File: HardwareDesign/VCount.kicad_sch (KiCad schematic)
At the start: 10 parts, among them SW201 SW_DIP_x10, U202 GAL22V10, U203 74ACT163, U204 74ACT163, U205 74ACT163

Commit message: don't incr upper VCOUNT counters unless HCEND is asserted
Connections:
- net HCOUNT_END: now also U204.10 (CET), U205.10 (CET)
- net at U204.15 (TC), U205.7 (CEP): no longer U205.10 (CET)
- net at U203.15 (TC), U204.7 (CEP): no longer U204.10 (CET)
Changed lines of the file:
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@@
-	)
-	(junction
-		(at 124.46 86.36)
-		(diameter 0)
-		(color 0 0 0 0)
 	)
 	(junction
@@
 	)
 	(junction
-		(at 72.39 86.36)
-		(diameter 0)
-		(color 0 0 0 0)
-	)
-	(junction
 		(at 143.51 76.2)
 		(diameter 0)
@@
 	)
 	(junction
+		(at 140.97 134.62)
+		(diameter 0)
+		(color 0 0 0 0)
+	)
+	(junction
 		(at 38.1 118.11)
 		(diameter 0)
@@
 	(junction
 		(at 143.51 132.08)
+		(diameter 0)
+		(color 0 0 0 0)
+	)
+	(junction
+		(at 88.9 134.62)
 		(diameter 0)
 		(color 0 0 0 0)
@@
 	(wire
 		(pts
-			(xy 93.98 88.9) (xy 72.39 88.9)
-		)
-		(stroke
-			(width 0)
-			(type default)
-		)
-	)
-	(wire
-		(pts
 			(xy 200.66 86.36) (xy 205.74 86.36)
 		)
@@
 	(wire
 		(pts
+			(xy 93.98 88.9) (xy 88.9 88.9)
+		)
+		(stroke
+			(width 0)
+			(type default)
+		)
+	)
+	(wire
+		(pts
 			(xy 66.04 91.44) (xy 66.04 118.11)
 		)
@@
 	(wire
 		(pts
-			(xy 124.46 86.36) (xy 124.46 88.9)
-		)
-		(stroke
-			(width 0)
-			(type default)
-		)
-	)
-	(wire
-		(pts
 			(xy 54.61 24.13) (xy 54.61 27.94)
 		)
@@
 	(wire
 		(pts
-			(xy 124.46 88.9) (xy 146.05 88.9)
-		)
-		(stroke
-			(width 0)
-			(type default)
-		)
-	)
-	(wire
-		(pts
 			(xy 91.44 132.08) (xy 143.51 132.08)
 		)
@@
 	(wire
 		(pts
+			(xy 140.97 88.9) (xy 140.97 134.62)
+		)
+		(stroke
+			(width 0)
+			(type default)
+		)
+	)
+	(wire
+		(pts
 			(xy 24.765 24.13) (xy 40.005 24.13)
 		)
@@
 		)
 	)
-	(wire
-		(pts
-			(xy 72.39 88.9) (xy 72.39 86.36)
-		)
-		(stroke
-			(width 0)
-			(type default)
-		)
-	)
 	(bus
 		(pts
@@
 		)
 	)
+	(wire
+		(pts
+			(xy 146.05 88.9) (xy 140.97 88.9)
+		)
+		(stroke
+			(width 0)
+			(type default)
+		)
+	)
 	(bus
 		(pts
@@
 	(wire
 		(pts
-			(xy 33.02 134.62) (xy 184.15 134.62)
+			(xy 33.02 134.62) (xy 88.9 134.62)
 		)
 		(stroke
@@
 	(wire
 		(pts
+			(xy 88.9 88.9) (xy 88.9 134.62)
+		)
+		(stroke
+			(width 0)
+			(type default)
+		)
+	)
+	(wire
+		(pts
 			(xy 205.74 119.38) (xy 201.93 119.38)
 		)
@@
 		)
 	)
+	(wire
+		(pts
+			(xy 140.97 134.62) (xy 184.15 134.62)
+		)
+		(stroke
+			(width 0)
+			(type default)
+		)
+	)
 	(bus
 		(pts
@@
 		)
 		(stroke
+			(width 0)
+			(type default)
+		)
+	)
+	(wire
+		(pts
+			(xy 88.9 134.62) (xy 140.97 134.62)
+		)
+		(stroke

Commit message: reverted previous VCount change; hw was correct
The TC a.k.a. "RCO" output only goes high if the
counter is at terminal count, AND the CET input
is high. Since the low-bit '163 in VCount has its
CET driven by HCOUNT_END, it only asserts TC/RCO
if HCOUNT_END is asserted, thus the cascaded counters
are never enabled if the low counter is not enabled.

This is good news since it means I don't need to
change the wiring of the prototype VCount module.

The change being reverted was not really wrong.
(I don't think it was wrong anyway.) However, I
think it's important for the schematics to be
100% consistent with the prototype hardware.
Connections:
- net HCOUNT_END: no longer U204.10 (CET), U205.10 (CET)
- net at U204.15 (TC), U205.7 (CEP): now also U205.10 (CET)
- net at U203.15 (TC), U204.7 (CEP): now also U204.10 (CET)
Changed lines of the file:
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@@
+	)
+	(junction
+		(at 72.39 86.36)
+		(diameter 0)
+		(color 0 0 0 0)
 	)
 	(junction
@@
 	)
 	(junction
-		(at 140.97 134.62)
+		(at 124.46 86.36)
 		(diameter 0)
 		(color 0 0 0 0)
@@
 	(junction
 		(at 143.51 132.08)
-		(diameter 0)
-		(color 0 0 0 0)
-	)
-	(junction
-		(at 88.9 134.62)
 		(diameter 0)
 		(color 0 0 0 0)
@@
 	(wire
 		(pts
-			(xy 93.98 88.9) (xy 88.9 88.9)
-		)
-		(stroke
-			(width 0)
-			(type default)
-		)
-	)
-	(wire
-		(pts
 			(xy 66.04 91.44) (xy 66.04 118.11)
 		)
@@
 	(wire
 		(pts
+			(xy 146.05 88.9) (xy 124.46 88.9)
+		)
+		(stroke
+			(width 0)
+			(type default)
+		)
+	)
+	(wire
+		(pts
 			(xy 106.68 104.14) (xy 106.68 106.68)
 		)
@@
 	(wire
 		(pts
-			(xy 140.97 88.9) (xy 140.97 134.62)
-		)
-		(stroke
-			(width 0)
-			(type default)
-		)
-	)
-	(wire
-		(pts
 			(xy 24.765 24.13) (xy 40.005 24.13)
 		)
@@
 	(wire
 		(pts
+			(xy 93.98 88.9) (xy 72.39 88.9)
+		)
+		(stroke
+			(width 0)
+			(type default)
+		)
+	)
+	(wire
+		(pts
 			(xy 200.66 86.36) (xy 200.66 78.74)
 		)
@@
 		)
 	)
-	(wire
-		(pts
-			(xy 146.05 88.9) (xy 140.97 88.9)
-		)
-		(stroke
-			(width 0)
-			(type default)
-		)
-	)
 	(bus
 		(pts
@@
 	(wire
 		(pts
-			(xy 33.02 134.62) (xy 88.9 134.62)
+			(xy 33.02 134.62) (xy 184.15 134.62)
 		)
 		(stroke
@@
 		)
 	)
+	(wire
+		(pts
+			(xy 124.46 88.9) (xy 124.46 86.36)
+		)
+		(stroke
+			(width 0)
+			(type default)
+		)
+	)
 	(bus
 		(pts
@@
 	(wire
 		(pts
-			(xy 88.9 88.9) (xy 88.9 134.62)
-		)
-		(stroke
-			(width 0)
-			(type default)
-		)
-	)
-	(wire
-		(pts
 			(xy 205.74 119.38) (xy 201.93 119.38)
 		)
@@
 		)
 	)
-	(wire
-		(pts
-			(xy 140.97 134.62) (xy 184.15 134.62)
-		)
-		(stroke
-			(width 0)
-			(type default)
-		)
-	)
 	(bus
 		(pts
@@
 	(wire
 		(pts
+			(xy 72.39 88.9) (xy 72.39 86.36)
+		)
+		(stroke
+			(width 0)
+			(type default)
+		)
+	)
+	(wire
+		(pts
 			(xy 30.48 88.9) (xy 33.02 88.9)
 		)
@@
 		)
 		(stroke
-			(width 0)
-			(type default)
-		)
-	)
-	(wire
-		(pts
-			(xy 88.9 134.62) (xy 140.97 134.62)
-		)
-		(stroke

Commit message: revise for accurat VCOUNT mods
Will need to double check these changes.
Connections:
- net GND: no longer U202.13 (I11)
- net HCOUNT_END: no longer U203.10 (CET)
- net VCOUNT_END renamed VCOUNT_ZERO
- new net VCOUNT_INCR: U202.13 (I11), U203.10 (CET)
- no-connect marks 8 -> 7
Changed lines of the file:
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@@
 	)
 	(no_connect
-		(at 241.3 101.6)
-	)
-	(no_connect
 		(at 171.45 76.2)
 	)
@@
 	(wire
 		(pts
+			(xy 184.15 119.38) (xy 205.74 119.38)
+		)
+		(stroke
+			(width 0)
+			(type default)
+		)
+	)
+	(wire
+		(pts
 			(xy 48.26 161.29) (xy 62.23 161.29)
 		)
@@
 	(wire
 		(pts
-			(xy 201.93 119.38) (xy 201.93 123.19)
-		)
-		(stroke
-			(width 0)
-			(type default)
-		)
-	)
-	(wire
-		(pts
 			(xy 77.47 176.53) (xy 95.25 176.53)
 		)
@@
 	(wire
 		(pts
-			(xy 184.15 134.62) (xy 184.15 116.84)
+			(xy 184.15 134.62) (xy 184.15 119.38)
 		)
 		(stroke
@@
 	(wire
 		(pts
-			(xy 241.3 114.3) (xy 251.46 114.3)
-		)
-		(stroke
-			(width 0)
-			(type default)
-		)
-	)
-	(wire
-		(pts
 			(xy 184.15 91.44) (xy 205.74 91.44)
 		)
@@
 		)
 	)
+	(wire
+		(pts
+			(xy 241.3 114.3) (xy 251.46 114.3)
+		)
+		(stroke
+			(width 0)
+			(type default)
+		)
+	)
 	(bus
 		(pts
@@
 	(wire
 		(pts
-			(xy 205.74 119.38) (xy 201.93 119.38)
-		)
-		(stroke
-			(width 0)
-			(type default)
-		)
-	)
-	(wire
-		(pts
 			(xy 72.39 83.82) (xy 72.39 86.36)
 		)
@@
 		)
 	)
-	(label "HCOUNT_END"
+	(label "VCOUNT_INCR"
 		(at 35.56 134.62 0)
 		(fields_autoplaced yes)
@@
 		)
 	)
+	(label "VCOUNT_INCR"
+		(at 186.69 119.38 0)
+		(fields_autoplaced yes)
+		(effects
+			(font
+				(size 1.27 1.27)
+			)
+			(justify left bottom)
+		)
+	)
 	(label "HCOUNT_END"
 		(at 186.69 116.84 0)
@@
 	(hierarchical_label "HCOUNT_END"
 		(shape input)
-		(at 30.48 88.9 180)
+		(at 184.15 116.84 180)
 		(fields_autoplaced yes)
 		(effects
@@
 		)
 	)
+	(hierarchical_label "VCOUNT_INCR"
+		(shape input)
+		(at 30.48 88.9 180)
+		(fields_autoplaced yes)
+		(effects
+			(font
+				(size 1.27 1.27)
+			)
+			(justify right)
+		)
+	)
 	(hierarchical_label "-RST"
 		(shape input)
@@
 		)
 	)
-	(hierarchical_label "PulseBegin"
+	(hierarchical_label "VCOUNT_ZERO"
 		(shape output)
-		(at 251.46 109.22 0)
+		(at 251.46 114.3 0)
 		(fields_autoplaced yes)
 		(effects
@@
 		)
 	)
-	(hierarchical_label "VC6"
+	(hierarchical_label "PulseBegin"
 		(shape output)
-		(at 200.66 38.1 0)
+		(at 251.46 109.22 0)
 		(fields_autoplaced yes)
 		(effects
@@
 		)
 	)
-	(hierarchical_label "VCOUNT_END"
+	(hierarchical_label "VC6"
 		(shape output)
-		(at 251.46 114.3 0)
+		(at 200.66 38.1 0)
 		(fields_autoplaced yes)
 		(effects
@@
 					(unit 1)
 				)
-			)
-		)
-	)
-	(symbol
-		(lib_name "GND_2")
-		(lib_id "power:GND")
-		(at 201.93 123.19 0)
-		(unit 1)
-		(exclude_from_sim no)
-		(in_bom yes)
-		(on_board yes)
-		(dnp no)
-		(fields_autoplaced yes)
-		(property "Reference" "#PWR036"
-			(at 201.93 129.54 0)
-			(effects
-				(font
-					(size 1.27 1.27)
-				)
-				(hide yes)
-			)
-		)
-		(property "Value" "GND"
-			(at 201.93 128.27 0)
-			(effects
-				(font
-					(size 1.27 1.27)
-				)
-			)
-		)
-		(property "Footprint" ""
-			(at 201.93 123.19 0)
-			(effects
-				(font
-					(size 1.27 1.27)
-				)
-				(hide yes)
-			)
-		)
-		(property "Datasheet" ""
-			(at 201.93 123.19 0)
-			(effects
-				(font
-					(size 1.27 1.27)
-				)
-				(hide yes)
-			)
-		)
-		(property "Description" "Power symbol creates a global label with name \"GND\" , ground"
-			(at 201.93 123.19 0)
-			(effects
-				(font
-					(size 1.27 1.27)
-				)
-				(hide yes)
-			)
-		)
-		(pin "1"
-		)
-		(instances
-			(project "HW_VGA"
-				(path "/c4bd4b39-993a-4195-805f-b4de6fa4aea5/ba60ce20-c64b-484d-a417-98010c724f04"
-					(reference "#PWR036")
-					(unit 1)
-				)

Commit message: add backplane connector to main sheet
Also tidied up a few details related to hardware
changes needed for accurate VCOUNT during horizontal
visibility.
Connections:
- net VCOUNT_END: now reaches U202.19 (I/O17)
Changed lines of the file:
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@@
+	(wire
+		(pts
+			(xy 241.3 101.6) (xy 260.35 101.6)
+		)
+		(stroke
+			(width 0)
+			(type default)
+		)
+	)
 	(wire
 		(pts
@@
 		(fields_autoplaced yes)
 		(effects
+			(font
+				(size 1.27 1.27)
+			)
+			(justify left bottom)
+		)
+	)
+	(label "VCOUNT_END"
+		(at 243.84 101.6 0)
+		(fields_autoplaced yes)
+		(effects

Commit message: more updates to add changes from sim
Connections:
- net VEndActive: now reaches U202.20 (I/O18)
- no-connect marks 7 -> 6
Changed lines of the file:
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@@
 	)
 	(no_connect
-		(at 241.3 99.06)
-	)
-	(no_connect
 		(at 241.3 96.52)
 	)
@@
 	(wire
 		(pts
-			(xy 241.3 101.6) (xy 260.35 101.6)
+			(xy 241.3 101.6) (xy 251.46 101.6)
 		)
 		(stroke
@@
 	(wire
 		(pts
+			(xy 241.3 99.06) (xy 251.46 99.06)
+		)
+		(stroke
+			(width 0)
+			(type default)
+		)
+	)
+	(wire
+		(pts
 			(xy 184.15 38.1) (xy 200.66 38.1)
 		)
@@
 		)
 	)
-	(label "VCOUNT_END"
-		(at 243.84 101.6 0)
-		(fields_autoplaced yes)
-		(effects
-			(font
-				(size 1.27 1.27)
-			)
-			(justify left bottom)
-		)
-	)
 	(label "InitVC2"
 		(at 26.67 76.2 0)
@@
 		(fields_autoplaced yes)
 		(effects
+			(font
+				(size 1.27 1.27)
+			)
+			(justify left)
+		)
+	)
+	(hierarchical_label "VCOUNT_END"
+		(shape output)
+		(at 251.46 101.6 0)
+		(fields_autoplaced yes)
+		(effects
+			(font
+				(size 1.27 1.27)
+			)
+			(justify left)
+		)
+	)
+	(hierarchical_label "VEndActive"
+		(shape output)
+		(at 251.46 99.06 0)
+		(fields_autoplaced yes)
+		(effects

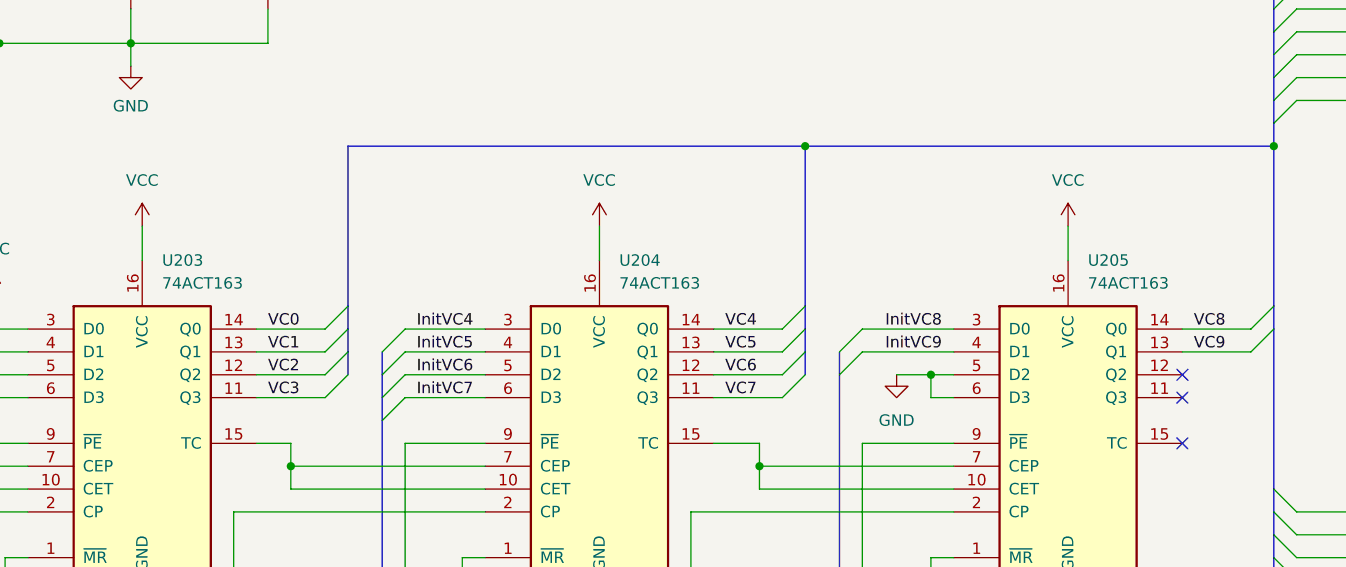
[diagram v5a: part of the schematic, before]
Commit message: use 74ALS163 rather than 74ACT163
The prototype did not work reliably with 74ACT163 counters,
but did work correctly with 74ALS163 counters.
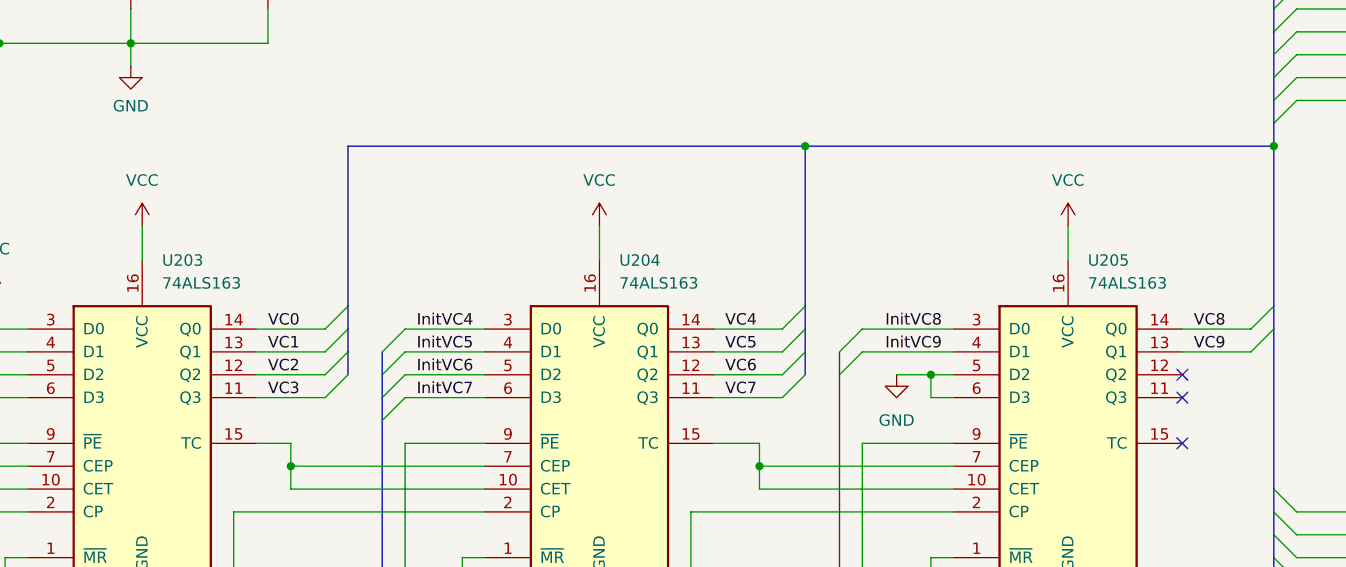
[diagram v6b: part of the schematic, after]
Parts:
- U203, U204, U205: value 74ACT163 -> 74ALS163
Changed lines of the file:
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@@
 			)
 		)
-		(property "Value" "74ACT163"
+		(property "Value" "74ALS163"
 			(at 160.9441 66.04 0)
 			(effects
@@
 			)
 		)
-		(property "Value" "74ACT163"
+		(property "Value" "74ALS163"
 			(at 58.0741 66.04 0)
 			(effects
@@
 			)
 		)
-		(property "Value" "74ACT163"
+		(property "Value" "74ALS163"
 			(at 108.8741 66.04 0)
 			(effects
